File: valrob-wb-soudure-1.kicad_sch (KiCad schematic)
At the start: 31 parts, among them J1 Conn_01x03, J2 Conn_01x06, J4 Conn_01x02, J5 Conn_01x02, J6 Conn_01x02, J7 Conn_01x02, Q1 2N7000, SW2 SW_Push, SW3 SW_Push, SW4 SW_Push, SW5 SW_Push

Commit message: schem: add title
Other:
- company: (none) -> Valrobotik
- title: (none) -> Valrob WB Soudure 1
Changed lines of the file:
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@@
 	(generator_version "10.0")
 	(paper "A4")
+	(title_block
+		(title "Valrob WB Soudure 1")
+		(date "2026-09-06")
+		(rev "01")
+		(company "Valrobotik")
+	)
 	(rectangle
 		(start 91.44 102.87)

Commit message: schem: renumber
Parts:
- J4: renamed from J6; now in the parts list
- J5: renamed from J7; now in the parts list
- renumbered D8 to D4, D9 to D5, D4 to D6, D5 to D7, D6 to D8, D7 to D9, J4 to J3, J5 to J6, R7 to R3, R8 to R4, R3 to R5, R4 to R6, R5 to R7, R6 to R8, SW5 to SW1, SW3 to SW2, SW4 to SW3, SW2 to SW4

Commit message: schem: update pot footprint
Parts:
- RV1: footprint Package_SO:TSSOP-20_4.4x6.5mm_P0.65mm -> Potentiometer_THT:Potentiometer_Alps_RK09Y11_Single_Horizontal; Basic (none) -> Z; JLCPCB Part # (none) -> C470717; Manufacturer (none) -> ALPSALPINE; Manufacturer Part Number (none) -> RK09Y11L0001
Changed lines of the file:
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@@
 			)
 		)
-		(property "Footprint" "Package_SO:TSSOP-20_4.4x6.5mm_P0.65mm"
+		(property "Footprint" "Potentiometer_THT:Potentiometer_Alps_RK09Y11_Single_Horizontal"
 			(at 118.11 119.38 0)
 			(hide yes)
@@
 			(at 118.11 119.38 0)
 			(hide yes)
+			(show_name no)
+			(do_not_autoplace no)
+			(effects
+				(font
+					(size 1.27 1.27)
+				)
+			)
+		)
+		(property "Basic" "Z"
+			(at 118.11 119.38 0)
+			(hide yes)
+			(show_name no)
+			(do_not_autoplace no)
+			(effects
+				(font
+					(size 1.27 1.27)
+				)
+			)
+		)
+		(property "JLCPCB Part #" "C470717"
+			(at 118.11 119.38 0)
+			(hide yes)
+			(show_name no)
+			(do_not_autoplace no)
+			(effects
+				(font
+					(size 1.27 1.27)
+				)
+			)
+		)
+		(property "Manufacturer" "ALPSALPINE"
+			(at 118.11 119.38 0)
+			(hide yes)
+			(show_name no)
+			(do_not_autoplace no)
+			(effects
+				(font
+					(size 1.27 1.27)
+				)
+			)
+		)
+		(property "Manufacturer Part Number" "RK09Y11L0001"
+			(at 118.11 119.38 0)
+			(hide yes)

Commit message: pcb: initial layout
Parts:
- J2: footprint Package_TO_SOT_THT:TO-92_Inline -> Connector_JST:JST_XH_B6B-XH-A_1x06_P2.50mm_Vertical
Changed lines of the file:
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@@
 			)
 		)
-		(property "Footprint" "Package_TO_SOT_THT:TO-92_Inline"
+		(property "Footprint" "Connector_JST:JST_XH_B6B-XH-A_1x06_P2.50mm_Vertical"
 			(at 96.52 119.38 0)
 			(hide yes)

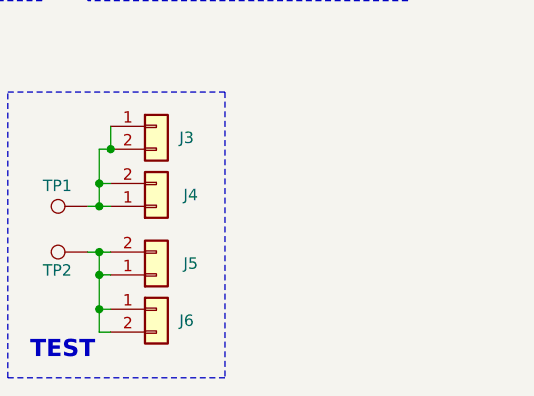
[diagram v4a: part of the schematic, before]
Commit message: schem/pcb: add M3 mouting holes
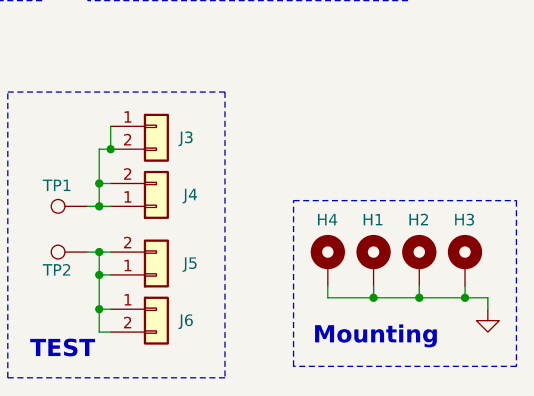
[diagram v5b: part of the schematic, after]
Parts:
- added H1, H2, H3, H4: MountingHole_Pad, MountingHole:MountingHole_3.2mm_M3_Pad_Via, symbol Mechanical:MountingHole_Pad
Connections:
- net GND: now also H1.1, H2.1, H3.1, H4.1
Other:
- note added: "Mounting"

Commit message: schem: add JST connectors parts #
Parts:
- J1: Basic (none) -> Z; JLCPCB Part # (none) -> C144394; Manufacturer (none) -> JST; Manufacturer Part Number (none) -> B3B-XH-A(LF)(SN)
- J2: Basic (none) -> Z; JLCPCB Part # (none) -> C144397; Manufacturer (none) -> JST; Manufacturer Part Number (none) -> B6B-XH-A(LF)(SN)
- J3, J6: Basic (none) -> Z; JLCPCB Part # (none) -> C495685; Manufacturer (none) -> JST; Manufacturer Part Number (none) -> B2B-XH-A-R(LF)(SN)
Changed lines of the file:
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@@
 			)
 		)
+		(property "Basic" "Z"
+			(at 191.77 124.46 0)
+			(hide yes)
+			(show_name no)
+			(do_not_autoplace no)
+			(effects
+				(font
+					(size 1.27 1.27)
+				)
+			)
+		)
+		(property "JLCPCB Part #" "C495685"
+			(at 191.77 124.46 0)
+			(hide yes)
+			(show_name no)
+			(do_not_autoplace no)
+			(effects
+				(font
+					(size 1.27 1.27)
+				)
+			)
+		)
+		(property "Manufacturer" "JST"
+			(at 191.77 124.46 0)
+			(hide yes)
+			(show_name no)
+			(do_not_autoplace no)
+			(effects
+				(font
+					(size 1.27 1.27)
+				)
+			)
+		)
+		(property "Manufacturer Part Number" "B2B-XH-A-R(LF)(SN)"
+			(at 191.77 124.46 0)
+			(hide yes)
+			(show_name no)
+			(do_not_autoplace no)
+			(effects
+				(font
+					(size 1.27 1.27)
+				)
+			)
+		)
 		(pin "1"
 		)
@@
 			)
 		)
-		(property "Basic" ""
+		(property "Basic" "Z"
 			(at 71.12 62.23 0)
 			(hide yes)
@@
 			)
 		)
-		(property "JLCPCB Part #" ""
+		(property "JLCPCB Part #" "C144394"
 			(at 71.12 62.23 0)
 			(hide yes)
@@
 			)
 		)
-		(property "Manufacturer" ""
+		(property "Manufacturer" "JST"
 			(at 71.12 62.23 0)
 			(hide yes)
@@
 			)
 		)
-		(property "Manufacturer Part Number" ""
+		(property "Manufacturer Part Number" "B3B-XH-A(LF)(SN)"
 			(at 71.12 62.23 0)
 			(hide yes)
@@
 			)
 		)
+		(property "Basic" "Z"
+			(at 191.77 104.14 0)
+			(hide yes)
+			(show_name no)
+			(do_not_autoplace no)
+			(effects
+				(font
+					(size 1.27 1.27)
+				)
+			)
+		)
+		(property "JLCPCB Part #" "C495685"
+			(at 191.77 104.14 0)
+			(hide yes)
+			(show_name no)
+			(do_not_autoplace no)
+			(effects
+				(font
+					(size 1.27 1.27)
+				)
+			)
+		)
+		(property "Manufacturer" "JST"
+			(at 191.77 104.14 0)
+			(hide yes)
+			(show_name no)
+			(do_not_autoplace no)
+			(effects
+				(font
+					(size 1.27 1.27)
+				)
+			)
+		)
+		(property "Manufacturer Part Number" "B2B-XH-A-R(LF)(SN)"
+			(at 191.77 104.14 0)
+			(hide yes)
+			(show_name no)
+			(do_not_autoplace no)
+			(effects
+				(font
+					(size 1.27 1.27)
+				)
+			)
+		)
 		(pin "1"
 		)
@@
 			(at 96.52 119.38 0)
 			(hide yes)
+			(show_name no)
+			(do_not_autoplace no)
+			(effects
+				(font
+					(size 1.27 1.27)
+				)
+			)
+		)
+		(property "Basic" "Z"
+			(at 96.52 119.38 0)
+			(hide yes)
+			(show_name no)
+			(do_not_autoplace no)
+			(effects
+				(font
+					(size 1.27 1.27)
+				)
+			)
+		)
+		(property "JLCPCB Part #" "C144397"
+			(at 96.52 119.38 0)
+			(hide yes)
+			(show_name no)
+			(do_not_autoplace no)
+			(effects
+				(font
+					(size 1.27 1.27)
+				)
+			)
+		)
+		(property "Manufacturer" "JST"
+			(at 96.52 119.38 0)
+			(hide yes)
+			(show_name no)
+			(do_not_autoplace no)
+			(effects
+				(font
+					(size 1.27 1.27)
+				)
+			)
+		)
+		(property "Manufacturer Part Number" "B6B-XH-A(LF)(SN)"
+			(at 96.52 119.38 0)
+			(hide yes)

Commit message: schem: add WJ500V-5.08-2P to BOM
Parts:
- J4, J5: JLCPCB Part # (none) -> C8465; Manufacturer (none) -> KANGNEX; Manufacturer Part Number (none) -> WJ500V-5.08-2P
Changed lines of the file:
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@@
+			)
+		)
+		(property "JLCPCB Part #" "C8465"
+			(at 191.77 120.65 0)
+			(hide yes)
+			(show_name no)
+			(do_not_autoplace no)
+			(effects
+				(font
+					(size 1.27 1.27)
+				)
+			)
+		)
+		(property "Manufacturer" "KANGNEX"
+			(at 191.77 120.65 0)
+			(hide yes)
+			(show_name no)
+			(do_not_autoplace no)
+			(effects
+				(font
+					(size 1.27 1.27)
+				)
+			)
+		)
+		(property "Manufacturer Part Number" "WJ500V-5.08-2P"
+			(at 191.77 120.65 0)
+			(hide yes)
+			(show_name no)
+			(do_not_autoplace no)
+			(effects
+				(font
+					(size 1.27 1.27)
+				)
 			)
 		)
@@
 			(at 191.77 113.03 0)
 			(hide yes)
+			(show_name no)
+			(do_not_autoplace no)
+			(effects
+				(font
+					(size 1.27 1.27)
+				)
+			)
+		)
+		(property "JLCPCB Part #" "C8465"
+			(at 191.77 113.03 0)
+			(hide yes)
+			(show_name no)
+			(do_not_autoplace no)
+			(effects
+				(font
+					(size 1.27 1.27)
+				)
+			)
+		)
+		(property "Manufacturer" "KANGNEX"
+			(at 191.77 113.03 0)
+			(hide yes)
+			(show_name no)
+			(do_not_autoplace no)
+			(effects
+				(font
+					(size 1.27 1.27)
+				)
+			)
+		)
+		(property "Manufacturer Part Number" "WJ500V-5.08-2P"
+			(at 191.77 113.03 0)
+			(hide yes)
